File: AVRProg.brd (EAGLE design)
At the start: 50.2 x 21 mm, 23 parts, among them IC2 LD111733, IC3 ATMEGA8, J1 Program, J2 Slow Clock, J3 USB, J4 ISP Target, J5 VDD Select, Q1 12 MHz

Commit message: foo
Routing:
- net VDD: track 76.8 -> 77.4 mm
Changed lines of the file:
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@@
 <param name="mtCopper" value="0.035mm 0.035mm 0.035mm 0.035mm 0.035mm 0.035mm 0.035mm 0.035mm 0.035mm 0.035mm 0.035mm 0.035mm 0.035mm 0.035mm 0.035mm 0.035mm"/>
 <param name="mtIsolate" value="1.5mm 0.15mm 0.2mm 0.15mm 0.2mm 0.15mm 0.2mm 0.15mm 0.2mm 0.15mm 0.2mm 0.15mm 0.2mm 0.15mm 0.2mm"/>
-<param name="mdWireWire" value="10mil"/>
+<param name="mdWireWire" value="8mil"/>
 <param name="mdWirePad" value="10mil"/>
 <param name="mdWireVia" value="10mil"/>
@@
 <contactref element="IC3" pad="3"/>
 <contactref element="IC3" pad="5"/>
+<via x="3.4925" y="15.24" extent="1-16" drill="0.6"/>
+<via x="2.54" y="14.605" extent="1-16" drill="0.6"/>
+<via x="8.89" y="15.24" extent="1-16" drill="0.6"/>
+<via x="7.9375" y="14.605" extent="1-16" drill="0.6"/>
+<via x="7.9375" y="5.715" extent="1-16" drill="0.6"/>
+<via x="8.89" y="6.35" extent="1-16" drill="0.6"/>
+<via x="3.4925" y="6.35" extent="1-16" drill="0.6"/>
+<via x="2.54" y="5.715" extent="1-16" drill="0.6"/>
 </signal>
 <signal name="+5V">
@@
 <wire x1="4.6975" y1="3.745" x2="5.715" y2="4.7625" width="0.3048" layer="1"/>
 <via x="5.715" y="4.7625" extent="1-16" drill="0.4"/>
-<wire x1="5.715" y1="4.7625" x2="8.89" y2="7.9375" width="0.3048" layer="16"/>
-<wire x1="8.89" y1="7.9375" x2="11.43" y2="7.9375" width="0.3048" layer="16"/>
+<wire x1="7.9375" y1="7.9375" x2="11.43" y2="7.9375" width="0.3048" layer="16"/>
 <wire x1="37.338" y1="14.4145" x2="34.671" y2="14.4145" width="0.4064" layer="1"/>
 <wire x1="34.671" y1="14.4145" x2="33.42" y2="13.1635" width="0.4064" layer="1"/>
@@
 <wire x1="33.42" y1="11.5951" x2="33.42" y2="13.1635" width="0.4064" layer="1"/>
 <wire x1="31.82" y1="11.5951" x2="31.82" y2="10.0395" width="0.4064" layer="1"/>
+<wire x1="7.9375" y1="7.9375" x2="5.715" y2="5.715" width="0.3048" layer="16"/>
+<wire x1="5.715" y1="5.715" x2="5.715" y2="4.7625" width="0.3048" layer="16"/>
 </signal>
 <signal name="N$138">

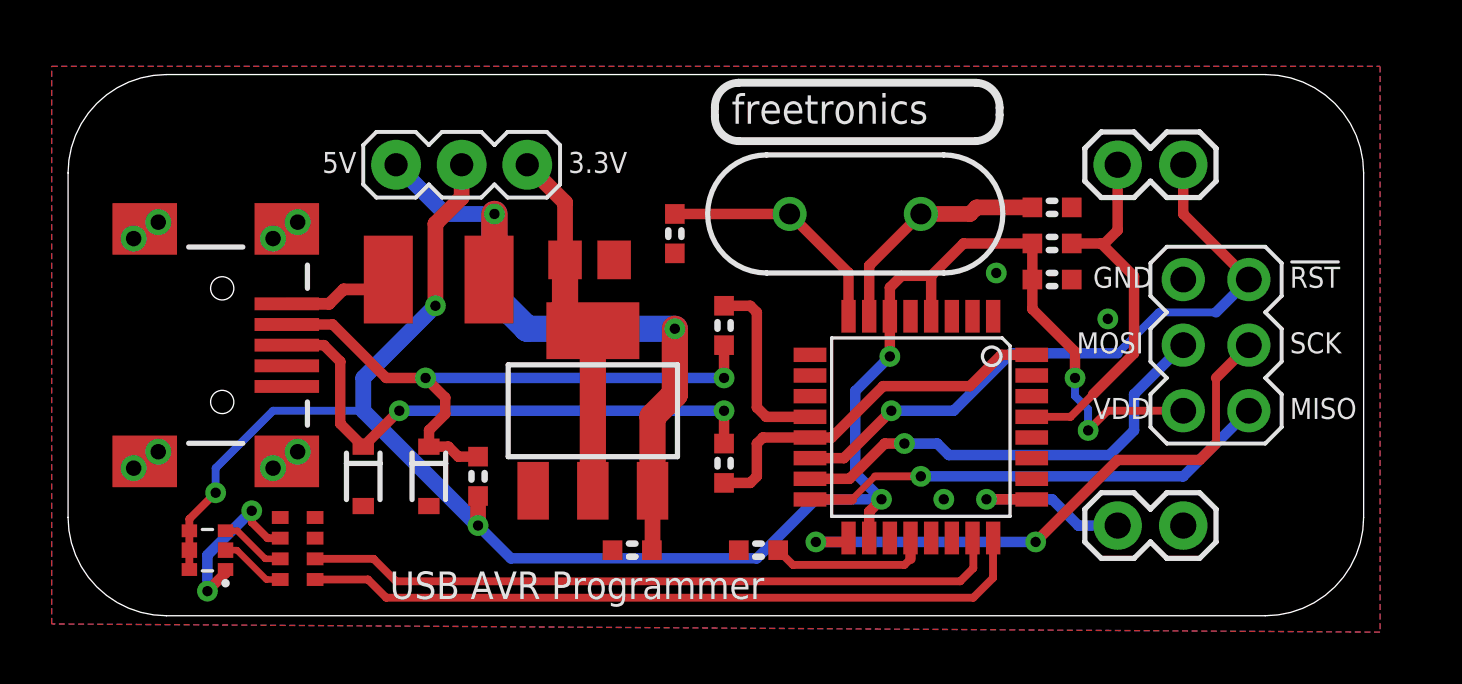
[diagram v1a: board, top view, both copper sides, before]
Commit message: changed zeners to miniMELF, moved jumpers to increase clearance around ISP header, added 10uF cap on 5V rail.
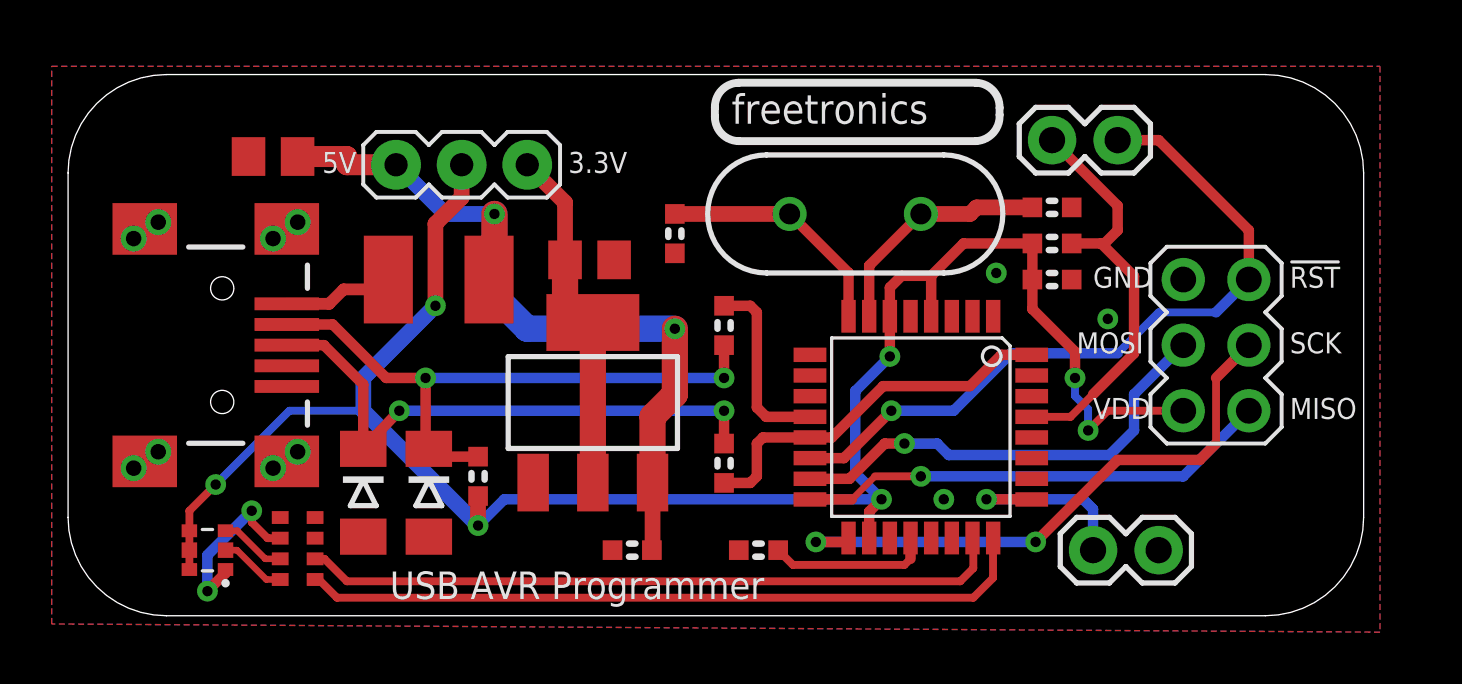
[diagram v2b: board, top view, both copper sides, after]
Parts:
- removed IC2: LD111733, freetronics-luke:SOT-223
- added C7: 10uF, freetronics-jon:C0805
- added IC1: LD111733, freetronics-luke:SOT-223
- ZD1, ZD2: device freetronics-luke:SOD-323 -> freetronics-luke:MINIMELF
- moved J1 2.71 mm to (39.4, 18.4)
- moved J2 1.35 mm to (41.0, 2.54)
- moved ZD1 0.63 mm to (14.0, 4.76)
- moved ZD2 0.63 mm to (11.4, 4.76)
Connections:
- net +3V3: now also IC1.2, IC1.4; no longer IC2.2, IC2.4
- net +5V: now also C7.1, IC1.3; no longer IC2.3
- net GND: now also C7.2, IC1.1; no longer IC2.1
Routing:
- net +5V: track 28.2 -> 32.4 mm
- net !RESET_OUT: track 25.4 -> 28.3 mm
- net !RESET: track 14.3 -> 16.3 mm
- net VDD: track 77.4 -> 76.0 mm

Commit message: foo
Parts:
- removed IC3: ATMEGA8, freetronics-luke:TQFP32-08
- added C8: 100nF, freetronics-master-v1:0603
- added IC2: LD111733, freetronics-luke:SOT-223
- C4, C6: value 100nF -> 10uF; device freetronics-master-v1:0603 -> freetronics-jon:C0805
- C5: value 10uF -> 100nF; device freetronics-jon:C0805 -> freetronics-master-v1:0603
- IC1: value LD111733 -> ATMEGA8; device freetronics-luke:SOT-223 -> freetronics-luke:TQFP32-08
- J2: value Slow Clock -> Slow clock
- moved C6 20.6 mm to (7.94, 17.8)
- moved C5 17.9 mm to (38.1, 13.0)
- moved C4 15.5 mm to (23.5, 18.1), turned to 90 degrees
- moved IC1 12.7 mm to (33.0, 7.30), turned to 270 degrees
- moved C7 12.6 mm to (20.2, 14.7), turned to 0 degrees
- moved J5 1.91 mm to (15.2, 19.4)
- moved J1 0.95 mm to (39.4, 19.4), turned to 0 degrees
- moved J2 0.95 mm to (41.0, 1.59), turned to 180 degrees
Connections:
- net !RESET: now also IC1.29, J1.1; no longer IC3.29, J1.2
- net !RESET_OUT: now also IC1.14, J1.2; no longer IC3.14, J1.1
- net +3V3: now also C7.1, IC2.2, IC2.4; no longer C5.1, IC1.2, IC1.4
- net +5V: now also C8.1, IC2.3; no longer C7.1, IC1.3
- net D+: now also IC1.13, IC1.32; no longer IC3.13, IC3.32
- net D-: now also IC1.12; no longer IC3.12
- net GND: now also C8.2, IC1.21, IC1.3, IC1.5, IC2.1, J2.1; no longer IC1.1, IC3.21, IC3.3, IC3.5, J2.2
- net LED1: now also IC1.23; no longer IC3.23
- net LED2: now also IC1.24; no longer IC3.24
- net MISO: now also IC1.16; no longer IC3.16
- net MOSI: now also IC1.15; no longer IC3.15
- net N$138: now also IC1.7; no longer IC3.7
- net N$139: now also IC1.8; no longer IC3.8
- net N$142: now also IC1.20; no longer IC3.20
- net SCK: now also IC1.17; no longer IC3.17
- net SLOW_SCK: now also IC1.25, J2.2; no longer IC3.25, J2.1
- net VDD: now also C5.1, IC1.18, IC1.4, IC1.6; no longer IC3.18, IC3.4, IC3.6
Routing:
- net VDD: track 76.0 -> 91.6 mm, vias 7 -> 8
- net +5V: track 32.4 -> 34.6 mm
- net +3V3: track 14.2 -> 16.1 mm
- net !RESET: track 16.3 -> 17.2 mm
- net SLOW_SCK: track 7.63 -> 8.39 mm
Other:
- board size 50.2 x 21 mm -> 48.7 x 21 mm
- board text added: "B:Power"
- board text added: "G:Active"
- board text added: "Program"
- board text added: "R:Write"
- board text added: "Slow Clock"
- board text added: "VDD Select"

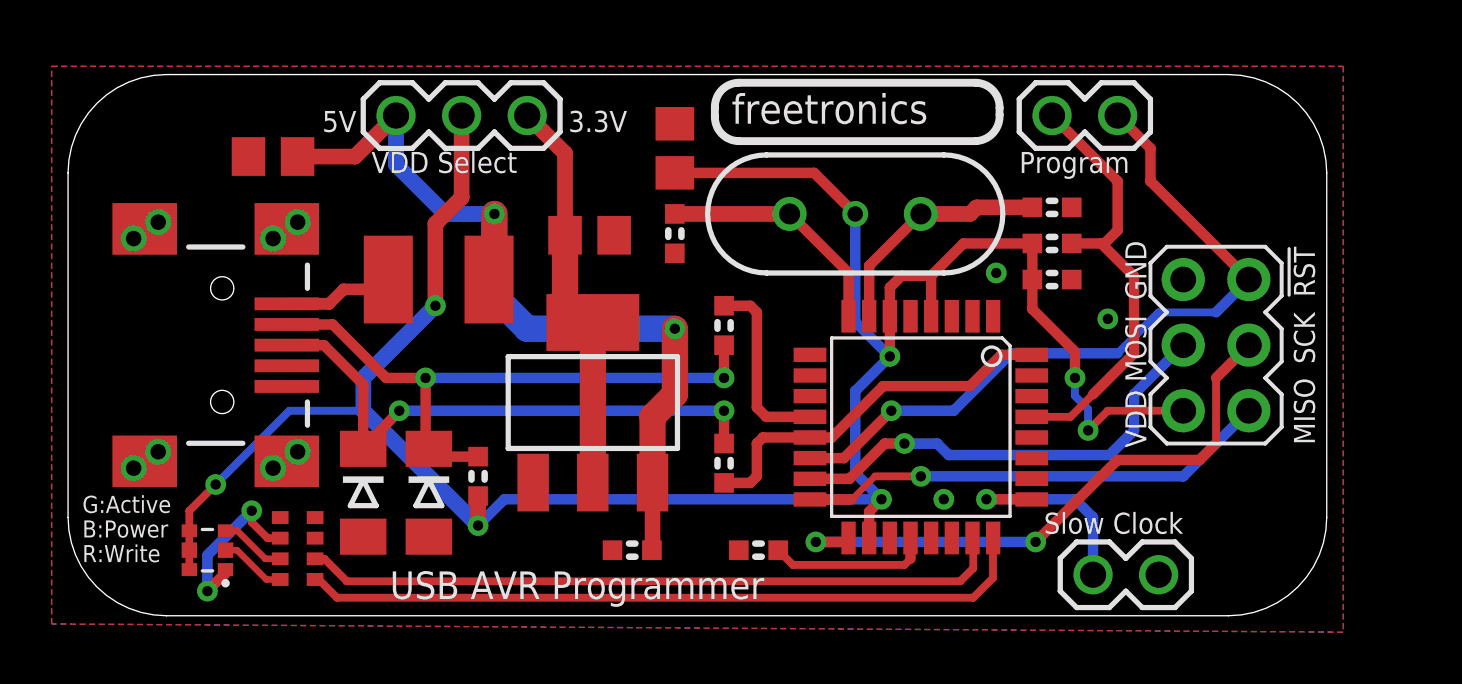
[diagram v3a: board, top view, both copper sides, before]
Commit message: Schematic and layout improvements
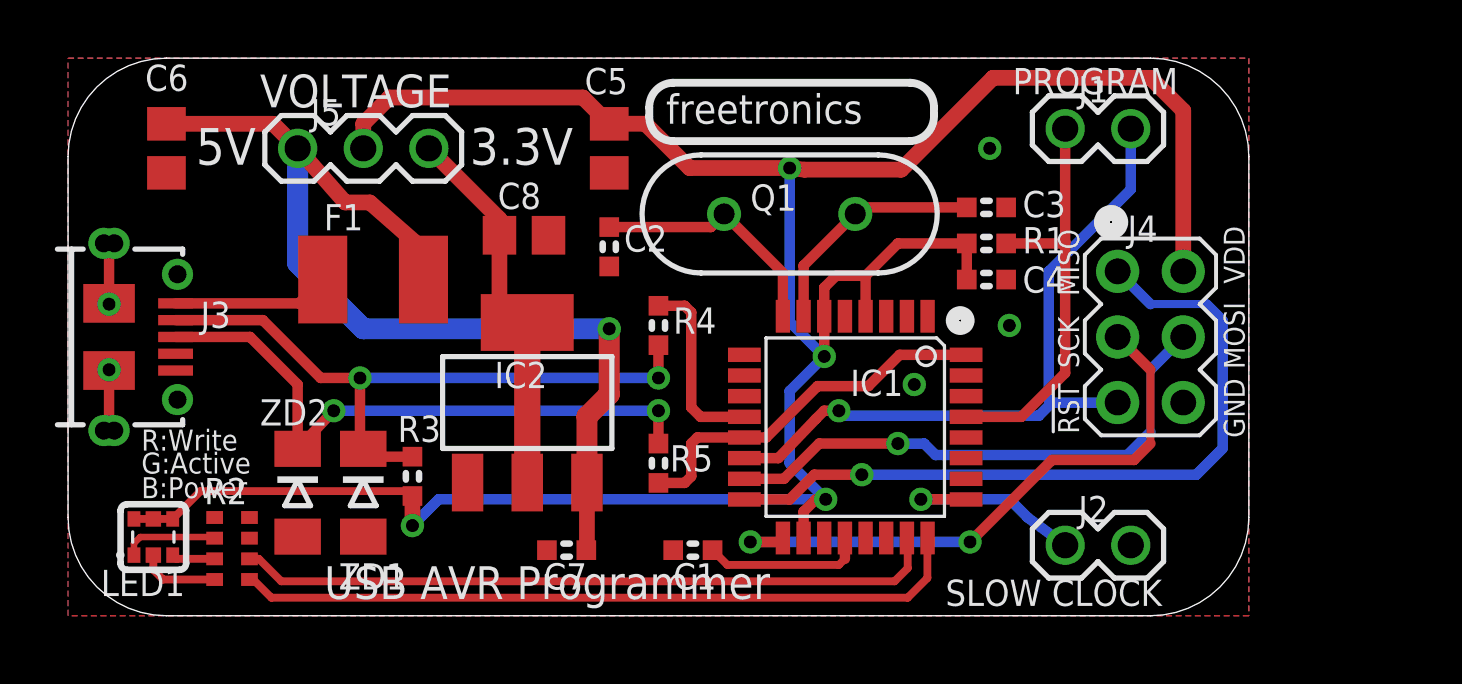
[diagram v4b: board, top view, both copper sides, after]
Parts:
- C1: value 100nF -> 100nF 0603
- C2: value 22p -> 22p 0603
- C3: value 22p -> 22p 0604
- C4, C7: value 10uF -> 100nF 0603; device freetronics-jon:C0805 -> freetronics-master-v1:0603
- C5, C8: value 100nF -> 10uF 10V 0805; device freetronics-master-v1:0603 -> freetronics-jon:C0805
- C6: value 10uF -> 10uF 10V 0805
- J3: device freetronics-luke:USB-MINIB-FT -> freetronics-jon:USB-MICROB-MB05PMXX
- R1: value 10k -> 10k 0604
- R3: value 2k2 -> 2K2 0603
- R4, R5: value 68R -> 68R 0603
- ZD1, ZD2: value 3V6 -> 3V6 0603
- moved C5 17.9 mm to (21.0, 18.1), turned to 270 degrees
- moved C4 13.1 mm to (35.6, 13.0), turned to 0 degrees
- moved C8 12.9 mm to (17.7, 14.7), turned to 0 degrees
- moved C7 12.2 mm to (19.3, 2.54), turned to 180 degrees
- moved C6 4.14 mm to (3.81, 18.1), turned to 270 degrees
- moved J5 4.02 mm to (11.4, 18.1)
- moved J3 3.13 mm to (1.59, 10.8), turned to 270 degrees
- moved C2 2.59 mm to (21.0, 14.3)
- moved J4 2.56 mm to (41.9, 10.8), turned to 270 degrees
- moved IC1 2.54 mm to (30.5, 7.30)
- moved F1 2.54 mm to (11.8, 13.0)
- moved R2 2.54 mm to (6.35, 2.60)
- moved ZD1 2.54 mm to (11.4, 4.76)
- moved C1 2.54 mm to (24.2, 2.54)
- moved C3 2.54 mm to (35.6, 15.8)
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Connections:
- net +3V3: now also C8.1; no longer C7.1
- net +5V: now also C7.1; no longer C8.1
- net GND: now also J3.FIX1, J3.FIX2, J3.PIN1, J3.PIN2, J3.TAB1, J3.TAB2; no longer J3.SH1, J3.SH2, J3.SH3, J3.SH4
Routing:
- net MISO: track 18.4 -> 29.1 mm
- net VDD: track 91.6 -> 99.8 mm, vias 8 -> 4
- net +5V: track 34.6 -> 39.7 mm, vias 2 -> 1
- net GND: track 0.00 -> 5.05 mm, vias 11 -> 5
- net MOSI: track 17.8 -> 21.0 mm
- net N$1: track 6.76 -> 3.70 mm, vias 2 -> 0
- net N$143: track 22.0 -> 23.9 mm
- net N$144: track 24.0 -> 25.8 mm
- net N$141: track 4.54 -> 6.08 mm
- net !RESET: track 17.2 -> 16.3 mm
- net N$3: track 2.57 -> 1.73 mm
- net !RESET_OUT: track 28.3 -> 27.5 mm
- net +3V3: track 16.1 -> 15.4 mm
- net N$2: track 2.59 -> 3.10 mm
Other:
- board size 48.7 x 21 mm -> 45.7 x 21.6 mm
- board text added: "(c) 2012 Freetronics Pty Ltd"
- board text added: "Copyright 2012 Freetronics Pty Ltd"
- board text added: "LED1"
- board text added: "Licensed under the TAPR"
- board text added: "Open Hardware License"
- board text added: "PROGRAM"
- board text added: "SLOW CLOCK"
- board text added: "USBasp AVR Programmer"
- board text added: "V1.0"
- board text added: "VOLTAGE"
- board text added: "www.tapr.org/OHL"
- board text removed: "(USBAsp compatible)"
- board text removed: "AVR Programmer"
- board text removed: "Program"
- board text removed: "Slow Clock"
- board text removed: "VDD Select"
